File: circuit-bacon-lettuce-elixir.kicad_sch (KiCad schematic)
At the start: 12 parts, among them J1 UART_MOD, J2 USB_CHG_DBG, J3 USB_DEV, SW1 RESET, U1 ESP32-C3-WROOM-02, U2 AP130-33Y

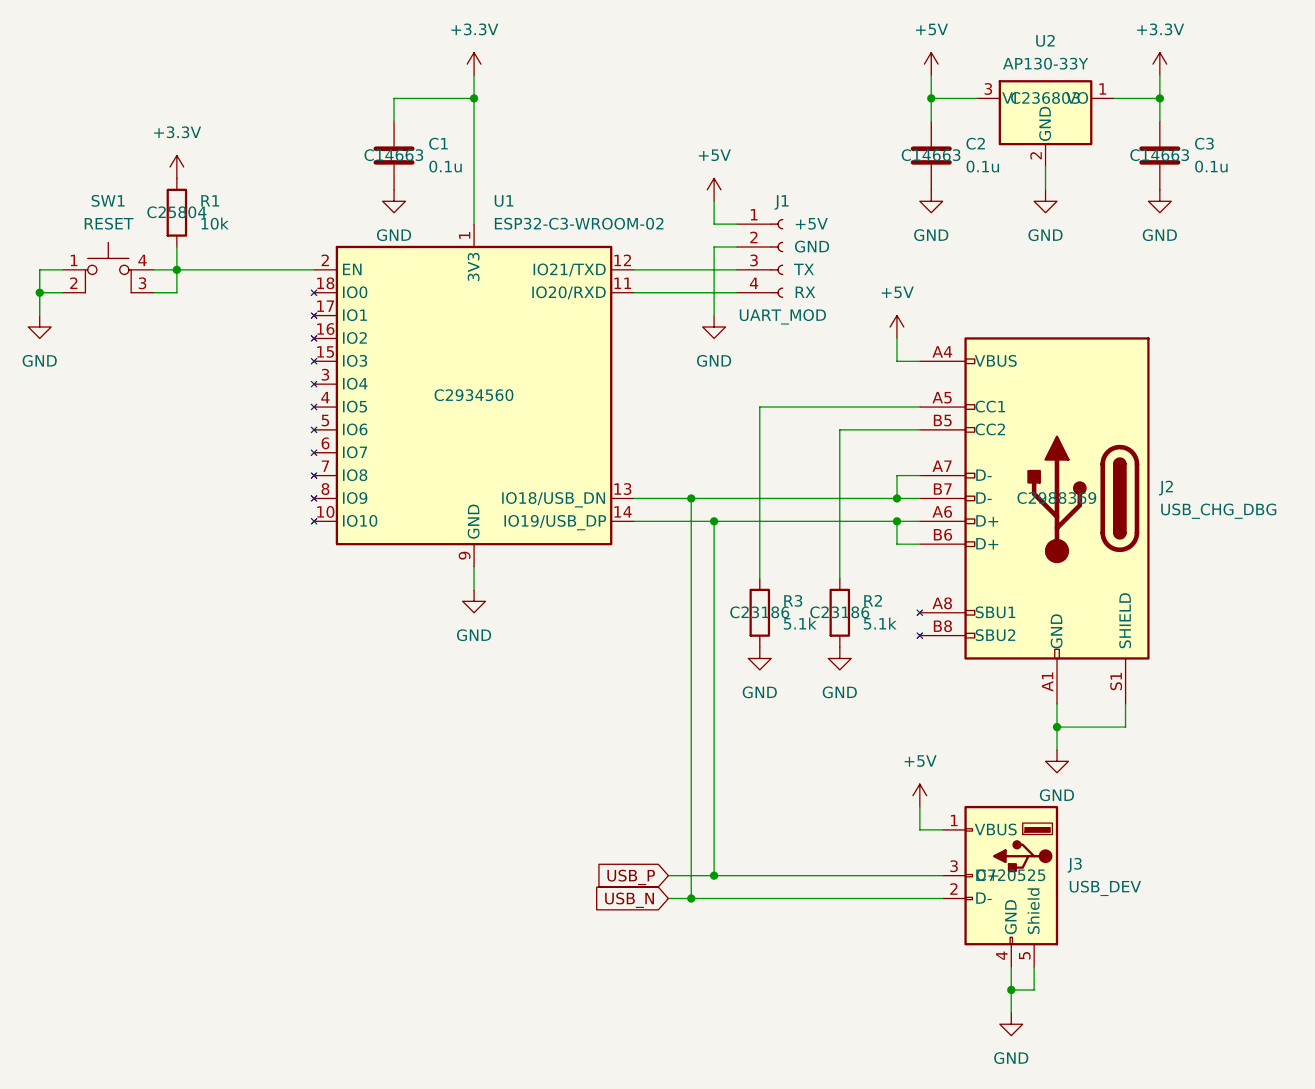
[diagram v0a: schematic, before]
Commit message: feature: 書き込み・給電コネクタをType-CからType-Aへ変更。
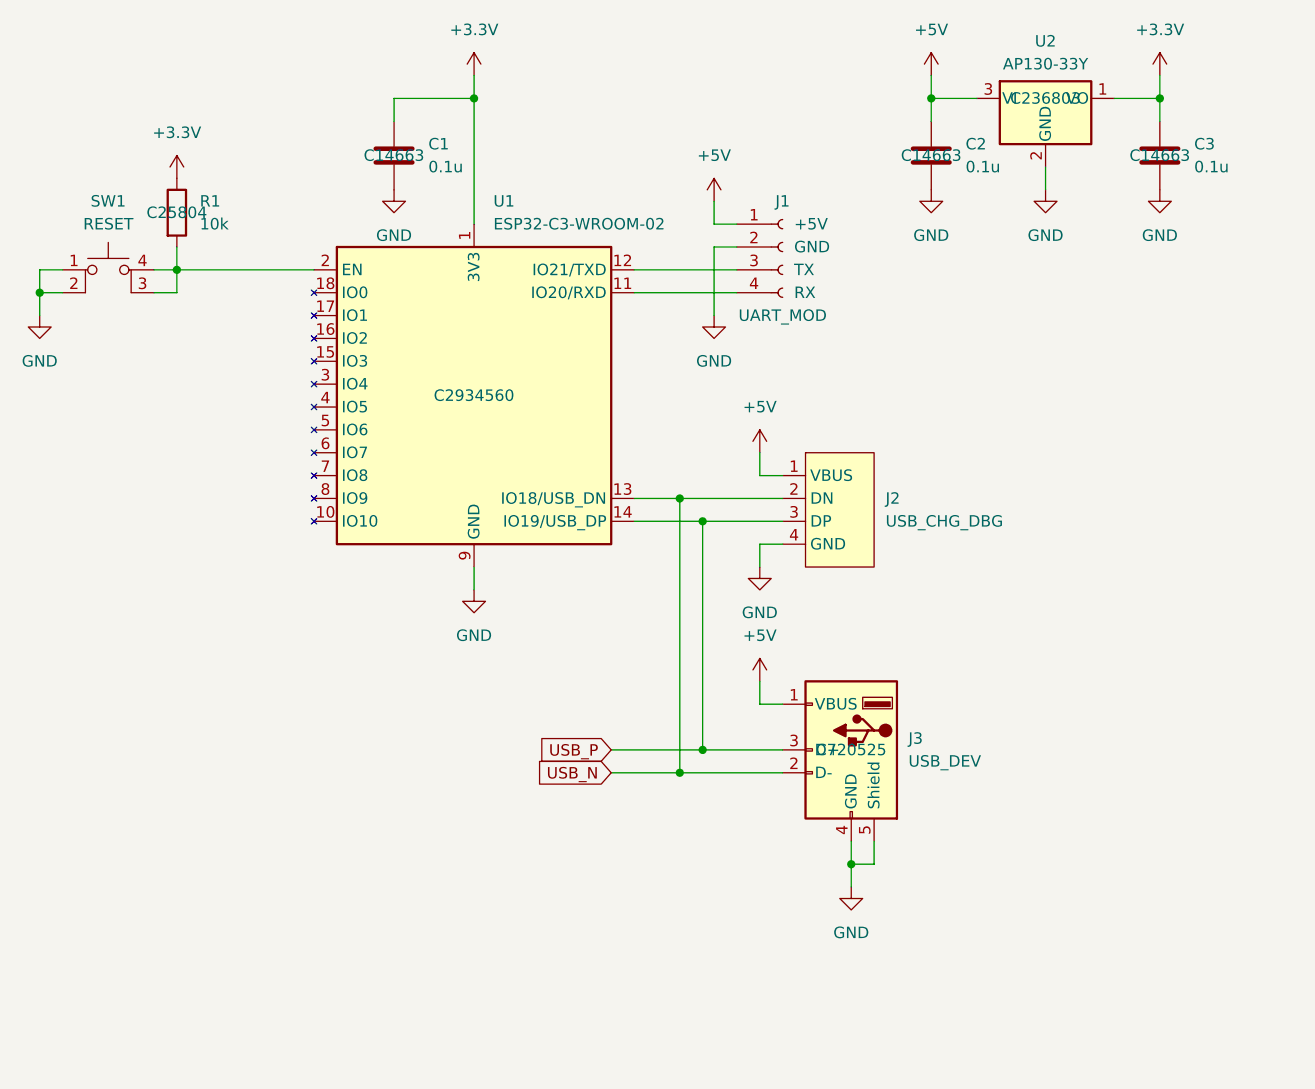
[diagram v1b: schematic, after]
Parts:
- removed R2, R3: 5.1k, Resistor_SMD:R_0603_1608Metric_Pad0.98x0.95mm_HandSolder, symbol Device:R
- J2: footprint Connector_USB:USB_C_Receptacle_G-Switch_GT-USB-7010ASV -> circuit-bacon-lettuce-elixir:PCB_USB_Connecter; LCSC PN C2988369 -> (none)
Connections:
- net +5V: now also J2.1 (VBUS); no longer J2.A4 (VBUS), J2.A9 (VBUS), J2.B4 (VBUS), J2.B9 (VBUS)
- net GND: now also J2.4 (GND); no longer J2.A1 (GND), J2.A12 (GND), J2.B1 (GND), J2.B12 (GND), J2.S1 (SHIELD)
- net USB_N: now also J2.2 (DN); no longer J2.A7 (D-), J2.B7 (D-)
- net USB_P: now also J2.3 (DP); no longer J2.A6 (D+), J2.B6 (D+)
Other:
- moved on the sheet: J3
